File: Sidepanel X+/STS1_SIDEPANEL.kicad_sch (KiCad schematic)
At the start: 3 parts, among them J1 Conn_02x04_Odd_Even, J2 Conn_02x02_Odd_Even

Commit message: Review Ready for V2.0
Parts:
- J1: value Conn_02x04_Odd_Even -> (none); footprint SamacSys:M808280842 -> (none)
- J2: value Conn_02x02_Odd_Even -> (none); footprint USER_Passiv:M80-8280442 -> (none)
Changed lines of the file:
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@@
     (in_bom yes) (on_board yes) (fields_autoplaced)
     (property "Reference" "J1" (id 0) (at 40.64 60.96 0))
-    (property "Value" "Conn_02x04_Odd_Even" (id 1) (at 40.64 63.5 0))
-    (property "Footprint" "SamacSys:M808280842" (id 2) (at 39.37 69.85 0)
+    (property "Value" "" (id 1) (at 40.64 63.5 0))
+    (property "Footprint" "" (id 2) (at 39.37 69.85 0)
       (effects (font (size 1.27 1.27)) hide)
     )
@@
     (in_bom yes) (on_board yes) (fields_autoplaced)
     (property "Reference" "J2" (id 0) (at 86.36 66.04 0))
-    (property "Value" "Conn_02x02_Odd_Even" (id 1) (at 86.36 68.58 0))
-    (property "Footprint" "USER_Passiv:M80-8280442" (id 2) (at 85.09 72.39 0)
+    (property "Value" "" (id 1) (at 86.36 68.58 0))
+    (property "Footprint" "" (id 2) (at 85.09 72.39 0)
       (effects (font (size 1.27 1.27)) hide)
     )
@@
     )
     (path "/4f87559b-6bba-4ff6-97a7-dad9a308db2d/934b6342-5d8d-49da-bf4f-f7fa77f16f34"
-      (reference "CUR1") (unit 1) (value "TMCS1101A3BQDT") (footprint "SOIC127P600X175-8N")
+      (reference "CUR1") (unit 1) (value "TMCS1101A3BQDT") (footprint "Package_SO:SOIC-8_3.9x4.9mm_P1.27mm")
     )
     (path "/4f87559b-6bba-4ff6-97a7-dad9a308db2d/a554cf31-0806-4740-ba0b-f0d59599f4ca"
@@
     )
     (path "/4f87559b-6bba-4ff6-97a7-dad9a308db2d/c6a198d2-e0e4-4d6d-8a2a-bdeb249501be"
-      (reference "DOUT1") (unit 1) (value "SMM4F5.0") (footprint "SamacSys:STMITE")
+      (reference "DOUT1") (unit 1) (value "SMM4F5.0") (footprint "Diode_SMD:D_0603_1608Metric")
     )
     (path "/9d03bb93-a9aa-424f-bd25-022f173efd1d/d9839939-8918-48f3-b4b2-d753b1d9a645"
-      (reference "IC1") (unit 1) (value "TMP112AQDRLRQ1") (footprint "SamacSys:SOTFL50P160X60-6N")
+      (reference "IC1") (unit 1) (value "TMP112AQDRLRQ1") (footprint "Package_TO_SOT_SMD:SOT-563")
     )
     (path "/7d4ab197-adca-450c-9fc5-7a95ff72b885"
-      (reference "J1") (unit 1) (value "Conn_02x04_Odd_Even") (footprint "SamacSys:M808280842")
+      (reference "J1") (unit 1) (value "Conn_02x04_Odd_Even") (footprint "STS_Connector:M808280842")
     )
     (path "/9272ccd5-e950-4f99-baec-47da7f19129b"
-      (reference "J2") (unit 1) (value "Conn_02x02_Odd_Even") (footprint "USER_Passiv:M80-8280442")
+      (reference "J2") (unit 1) (value "Conn_02x02_Odd_Even") (footprint "STS_Connector:M808280442")
     )
     (path "/4f87559b-6bba-4ff6-97a7-dad9a308db2d/bfe4e68f-4cef-4b31-adff-8df094bc3870"
-      (reference "L_IN1") (unit 1) (value "10u") (footprint "SamacSys:INDPM5650X530N")
+      (reference "L_IN1") (unit 1) (value "10u") (footprint "Inductor_SMD:L_0805_2012Metric")
     )
     (path "/4f87559b-6bba-4ff6-97a7-dad9a308db2d/679b2e27-da22-4f13-a86e-25be83598a10"
-      (reference "MPPT1") (unit 1) (value "SPV1040TTR") (footprint "SamacSys:SOP65P640X120-8N")
+      (reference "MPPT1") (unit 1) (value "SPV1040TTR") (footprint "Package_SO:TSSOP-8_4.4x3mm_P0.65mm")
     )
     (path "/6503b427-07c6-4391-8fa6-4757fb4daa6c"
@@
     )
     (path "/4f87559b-6bba-4ff6-97a7-dad9a308db2d/e7b54c2f-482e-4a97-841f-62a80e0193a8"
-      (reference "SC1") (unit 1) (value "Solar_Cell") (footprint "USER_Activ:3G30A_40x80")
+      (reference "SC1") (unit 1) (value "Solar_Cell") (footprint "STS_Connector:3G30A_40x80")
     )
     (path "/9d03bb93-a9aa-424f-bd25-022f173efd1d/a83d6342-0e16-4131-8bb9-e65e4d72dab0"
-      (reference "U1") (unit 1) (value "GUVA-C32SM") (footprint "USER_Optic:OLGA 2mm x 2,3mm")
-    )
-  )
+      (reference "U1") (unit 1) (value "GUVA-C32SM") (footprint "Package_SO:SO-4_4.4x3.6mm_P2.54mm")
+    )
+  )

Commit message: Further fixes, still some open
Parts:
- J1: value (none) -> Conn_02x04_Odd_Even; footprint (none) -> STS_Connector:M808280842
- J2: value (none) -> Conn_02x02_Odd_Even; footprint (none) -> STS_Connector:M808280442
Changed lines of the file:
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@@
     (in_bom yes) (on_board yes) (fields_autoplaced)
     (property "Reference" "J1" (id 0) (at 40.64 60.96 0))
-    (property "Value" "" (id 1) (at 40.64 63.5 0))
-    (property "Footprint" "" (id 2) (at 39.37 69.85 0)
+    (property "Value" "Conn_02x04_Odd_Even" (id 1) (at 40.64 63.5 0))
+    (property "Footprint" "STS_Connector:M808280842" (id 2) (at 39.37 69.85 0)
       (effects (font (size 1.27 1.27)) hide)
     )
@@
     (in_bom yes) (on_board yes) (fields_autoplaced)
     (property "Reference" "J2" (id 0) (at 86.36 66.04 0))
-    (property "Value" "" (id 1) (at 86.36 68.58 0))
-    (property "Footprint" "" (id 2) (at 85.09 72.39 0)
+    (property "Value" "Conn_02x02_Odd_Even" (id 1) (at 86.36 68.58 0))
+    (property "Footprint" "STS_Connector:M808280442" (id 2) (at 85.09 72.39 0)
       (effects (font (size 1.27 1.27)) hide)
     )

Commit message: Next fix
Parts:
- added TH1: Thermistor_NTC, Resistor_SMD:R_0805_2012Metric_Pad1.20x1.40mm_HandSolder, symbol Device:Thermistor_NTC
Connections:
- net GND: now also TH1.2
- net TEMP+: now also TH1.1
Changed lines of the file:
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@@
 (kicad_sch (version 20211123) (generator eeschema)
   (paper "A4")
+  (wire (pts (xy 31.75 88.9) (xy 31.75 92.71))
+    (stroke (width 0) (type default) (color 0 0 0 0))
+  )
+  (wire (pts (xy 31.75 100.33) (xy 31.75 103.505))
+    (stroke (width 0) (type default) (color 0 0 0 0))
+  )
   (wire (pts (xy 26.67 67.31) (xy 34.29 67.31))
     (stroke (width 0) (type default) (color 0 0 0 0))
@@
     (stroke (width 0) (type default) (color 0 0 0 0))
   )
+  (wire (pts (xy 31.75 88.9) (xy 38.735 88.9))
+    (stroke (width 0) (type default) (color 0 0 0 0))
+  )
   (wire (pts (xy 96.52 36.83) (xy 104.14 36.83))
     (stroke (width 0) (type default) (color 0 0 0 0))
@@
     (stroke (width 0) (type default) (color 0 0 0 0))
   )
+  (label "TEMP+" (at 38.735 88.9 180)
+    (effects (font (size 1.27 1.27)) (justify right bottom))
+  )
   (label "SC1_I+" (at 54.61 67.31 180)
     (effects (font (size 1.27 1.27)) (justify right bottom))
@@
   (label "SC2_I+" (at 82.55 41.91 180)
     (effects (font (size 1.27 1.27)) (justify right bottom))
+  )
+  (symbol (lib_id "power:GND") (at 31.75 103.505 0) (unit 1)
+    (in_bom yes) (on_board yes) (fields_autoplaced)
+    (property "Reference" "#PWR0107" (id 0) (at 31.75 109.855 0)
+      (effects (font (size 1.27 1.27)) hide)
+    )
+    (property "Value" "GND" (id 1) (at 31.75 108.585 0))
+    (property "Footprint" "" (id 2) (at 31.75 103.505 0)
+      (effects (font (size 1.27 1.27)) hide)
+    )
+    (property "Datasheet" "" (id 3) (at 31.75 103.505 0)
+      (effects (font (size 1.27 1.27)) hide)
+    )
+    (pin "1")
   )
   (symbol (lib_id "power:GND") (at 58.42 76.2 0) (unit 1)
@@
       (effects (font (size 1.27 1.27)) hide)
     )
+  )
+  (symbol (lib_id "Device:Thermistor_NTC") (at 31.75 96.52 0) (unit 1)
+    (in_bom yes) (on_board yes) (fields_autoplaced)
+    (property "Reference" "TH1" (id 0) (at 34.29 95.5674 0)
+      (effects (font (size 1.27 1.27)) (justify left))
+    )
+    (property "Value" "Thermistor_NTC" (id 1) (at 34.29 98.1074 0)
+      (effects (font (size 1.27 1.27)) (justify left))
+    )
+    (property "Footprint" "Resistor_SMD:R_0805_2012Metric_Pad1.20x1.40mm_HandSolder" (id 2) (at 31.75 95.25 0)
+      (effects (font (size 1.27 1.27)) hide)
+    )
+    (property "Datasheet" "~" (id 3) (at 31.75 95.25 0)
+      (effects (font (size 1.27 1.27)) hide)
+    )
+    (pin "1")
+    (pin "2")
   )
   (symbol (lib_id "Connector_Generic:Conn_02x04_Odd_Even") (at 39.37 69.85 0) (unit 1)
@@
       (reference "#PWR0106") (unit 1) (value "GND") (footprint "")
     )
+    (path "/10dfac46-9067-4751-a078-8b3b3c2c59bd"
+      (reference "#PWR0107") (unit 1) (value "GND") (footprint "")
+    )
     (path "/4f87559b-6bba-4ff6-97a7-dad9a308db2d/5bbe5da1-3bad-4b6d-b046-d5fbf4c349d2"
       (reference "#PWR0108") (unit 1) (value "GND") (footprint "")
@@
     )
     (path "/4f87559b-6bba-4ff6-97a7-dad9a308db2d/e7b54c2f-482e-4a97-841f-62a80e0193a8"
-      (reference "SC1") (unit 1) (value "Solar_Cell") (footprint "STS_Connector:3G30A_40x80")
+      (reference "SC1") (unit 1) (value "Solar_Cell") (footprint "STS_Solarcells:3G30A_40x80")
+    )
+    (path "/750cb84e-d795-4364-9358-ec0975478b7f"
+      (reference "TH1") (unit 1) (value "Thermistor_NTC") (footprint "Resistor_SMD:R_0805_2012Metric_Pad1.20x1.40mm_HandSolder")
     )
     (path "/9d03bb93-a9aa-424f-bd25-022f173efd1d/a83d6342-0e16-4131-8bb9-e65e4d72dab0"

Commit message: release_2.0, Ordered PCBs
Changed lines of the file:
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@@
     )
     (path "/4f87559b-6bba-4ff6-97a7-dad9a308db2d/c6a198d2-e0e4-4d6d-8a2a-bdeb249501be"
-      (reference "DOUT1") (unit 1) (value "SMM4F5.0") (footprint "Diode_SMD:D_0603_1608Metric")
+      (reference "DOUT1") (unit 1) (value "SMM4F5.0") (footprint "SamacSys:STMITE")
     )
     (path "/9d03bb93-a9aa-424f-bd25-022f173efd1d/d9839939-8918-48f3-b4b2-d753b1d9a645"
@@
     )
     (path "/4f87559b-6bba-4ff6-97a7-dad9a308db2d/bfe4e68f-4cef-4b31-adff-8df094bc3870"
-      (reference "L_IN1") (unit 1) (value "10u") (footprint "Inductor_SMD:L_0805_2012Metric")
+      (reference "L_IN1") (unit 1) (value "10u") (footprint "STS_Inductor_SMD:XAL6060103MEC")
     )
     (path "/4f87559b-6bba-4ff6-97a7-dad9a308db2d/679b2e27-da22-4f13-a86e-25be83598a10"

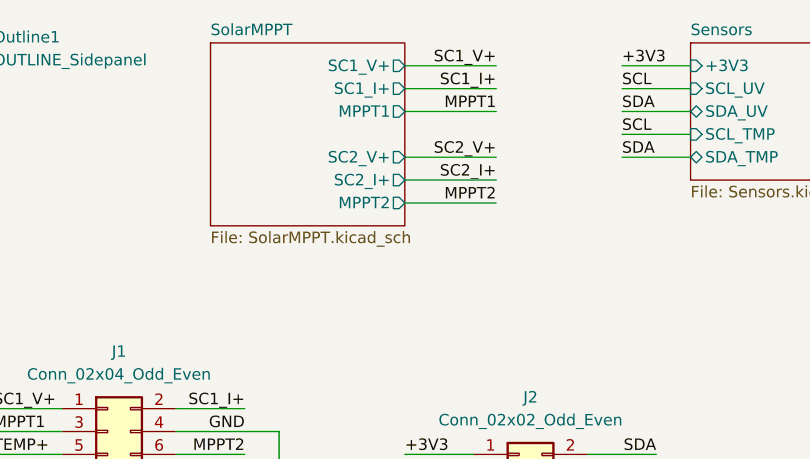
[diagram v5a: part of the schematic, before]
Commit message: Fixed some DRC errors.
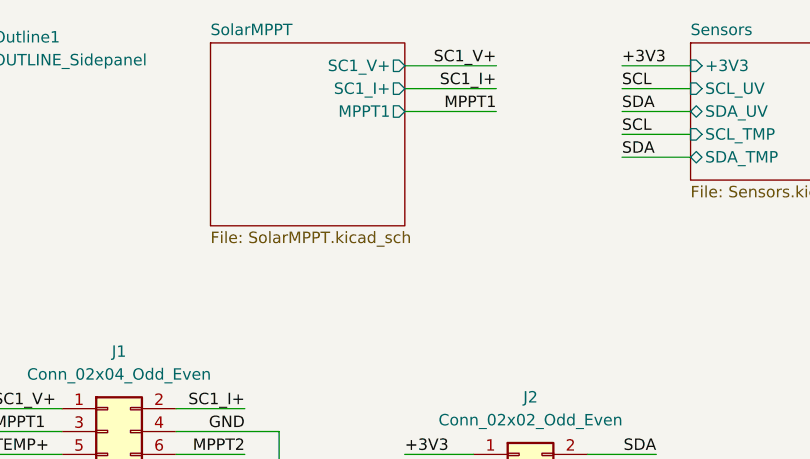
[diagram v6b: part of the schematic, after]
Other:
- sheet SolarMPPT ports: added none; removed MPPT2, SC2_I+, SC2_V+
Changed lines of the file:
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@@
-    (stroke (width 0) (type default) (color 0 0 0 0))
-  )
-  (wire (pts (xy 72.39 39.37) (xy 82.55 39.37))
     (stroke (width 0) (type default) (color 0 0 0 0))
   )
@@
     (stroke (width 0) (type default) (color 0 0 0 0))
   )
-  (wire (pts (xy 72.39 44.45) (xy 82.55 44.45))
-    (stroke (width 0) (type default) (color 0 0 0 0))
-  )
   (wire (pts (xy 96.52 34.29) (xy 104.14 34.29))
     (stroke (width 0) (type default) (color 0 0 0 0))
@@
     (stroke (width 0) (type default) (color 0 0 0 0))
   )
-  (wire (pts (xy 72.39 41.91) (xy 82.55 41.91))
-    (stroke (width 0) (type default) (color 0 0 0 0))
-  )
   (wire (pts (xy 46.99 69.85) (xy 58.42 69.85))
     (stroke (width 0) (type default) (color 0 0 0 0))
@@
     (effects (font (size 1.27 1.27)) (justify right bottom))
   )
-  (label "MPPT2" (at 82.55 44.45 180)
-    (effects (font (size 1.27 1.27)) (justify right bottom))
-  )
   (label "MPPT1" (at 26.67 69.85 0)
     (effects (font (size 1.27 1.27)) (justify left bottom))
@@
     (effects (font (size 1.27 1.27)) (justify right bottom))
   )
-  (label "SC2_V+" (at 82.55 39.37 180)
-    (effects (font (size 1.27 1.27)) (justify right bottom))
-  )
   (label "SC2_V+" (at 54.61 74.93 180)
     (effects (font (size 1.27 1.27)) (justify right bottom))
@@
   )
   (label "SDA" (at 100.33 72.39 180)
-    (effects (font (size 1.27 1.27)) (justify right bottom))
-  )
-  (label "SC2_I+" (at 82.55 41.91 180)
     (effects (font (size 1.27 1.27)) (justify right bottom))
   )
@@
       (effects (font (size 1.27 1.27)) (justify left top))
     )
-    (pin "SC2_I+" output (at 72.39 41.91 0)
-      (effects (font (size 1.27 1.27)) (justify right))
-    )
-    (pin "MPPT2" output (at 72.39 44.45 0)
-      (effects (font (size 1.27 1.27)) (justify right))
-    )
     (pin "SC1_V+" output (at 72.39 29.21 0)
       (effects (font (size 1.27 1.27)) (justify right))
@@
       (effects (font (size 1.27 1.27)) (justify right))
     )
-    (pin "SC2_V+" output (at 72.39 39.37 0)
-      (effects (font (size 1.27 1.27)) (justify right))
-    )

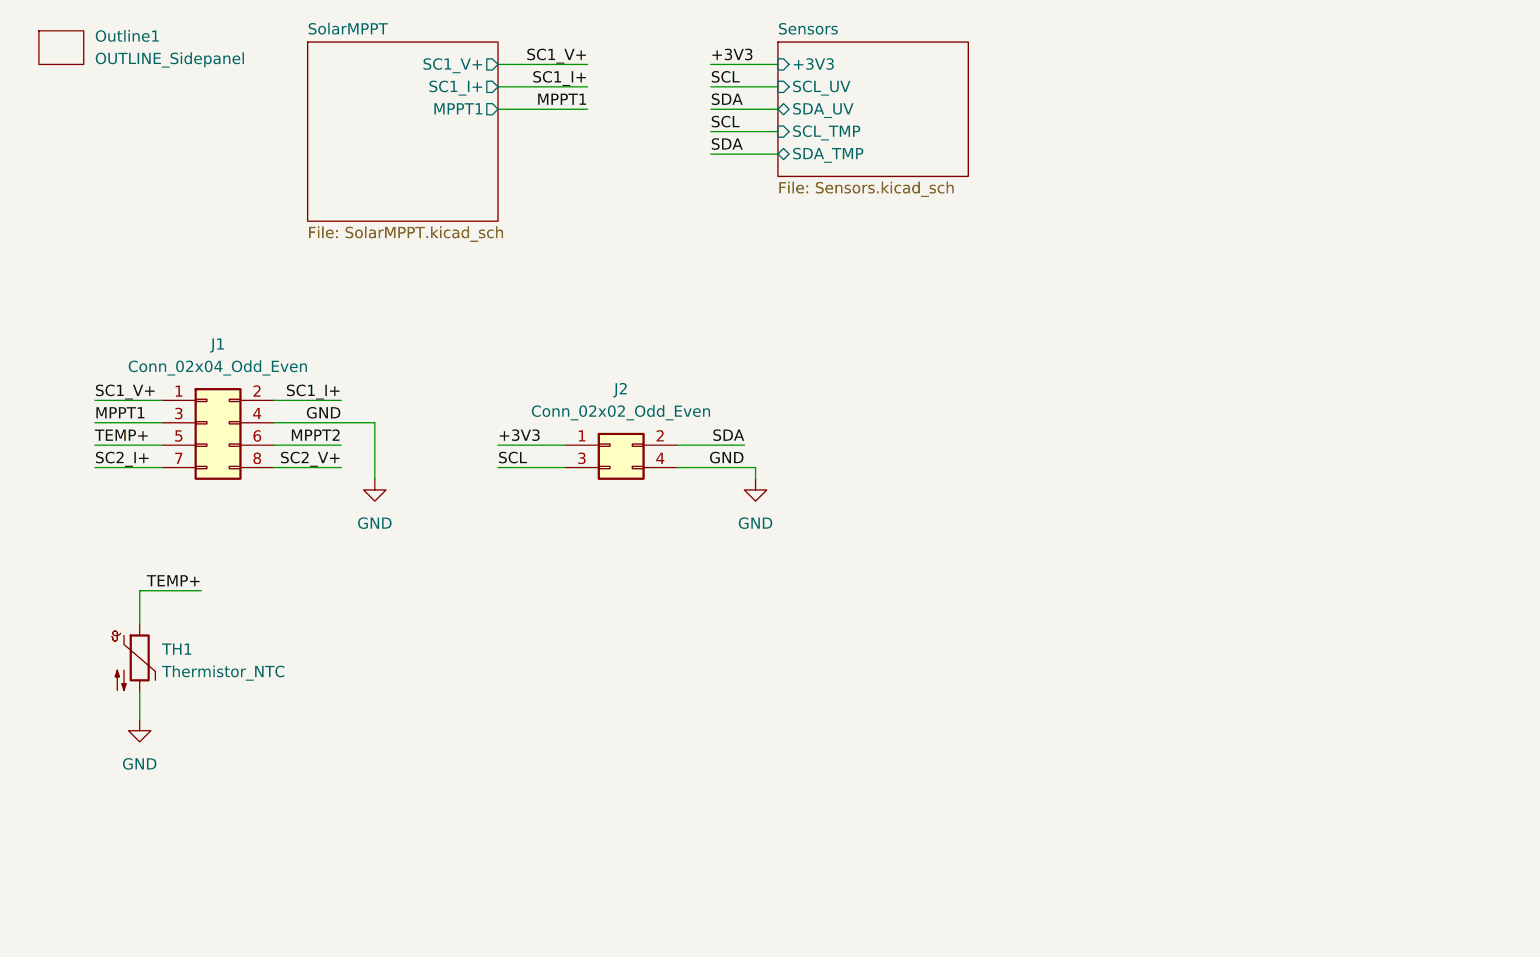
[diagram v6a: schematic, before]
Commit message: changes to the solar cells footprint, added camera mounts
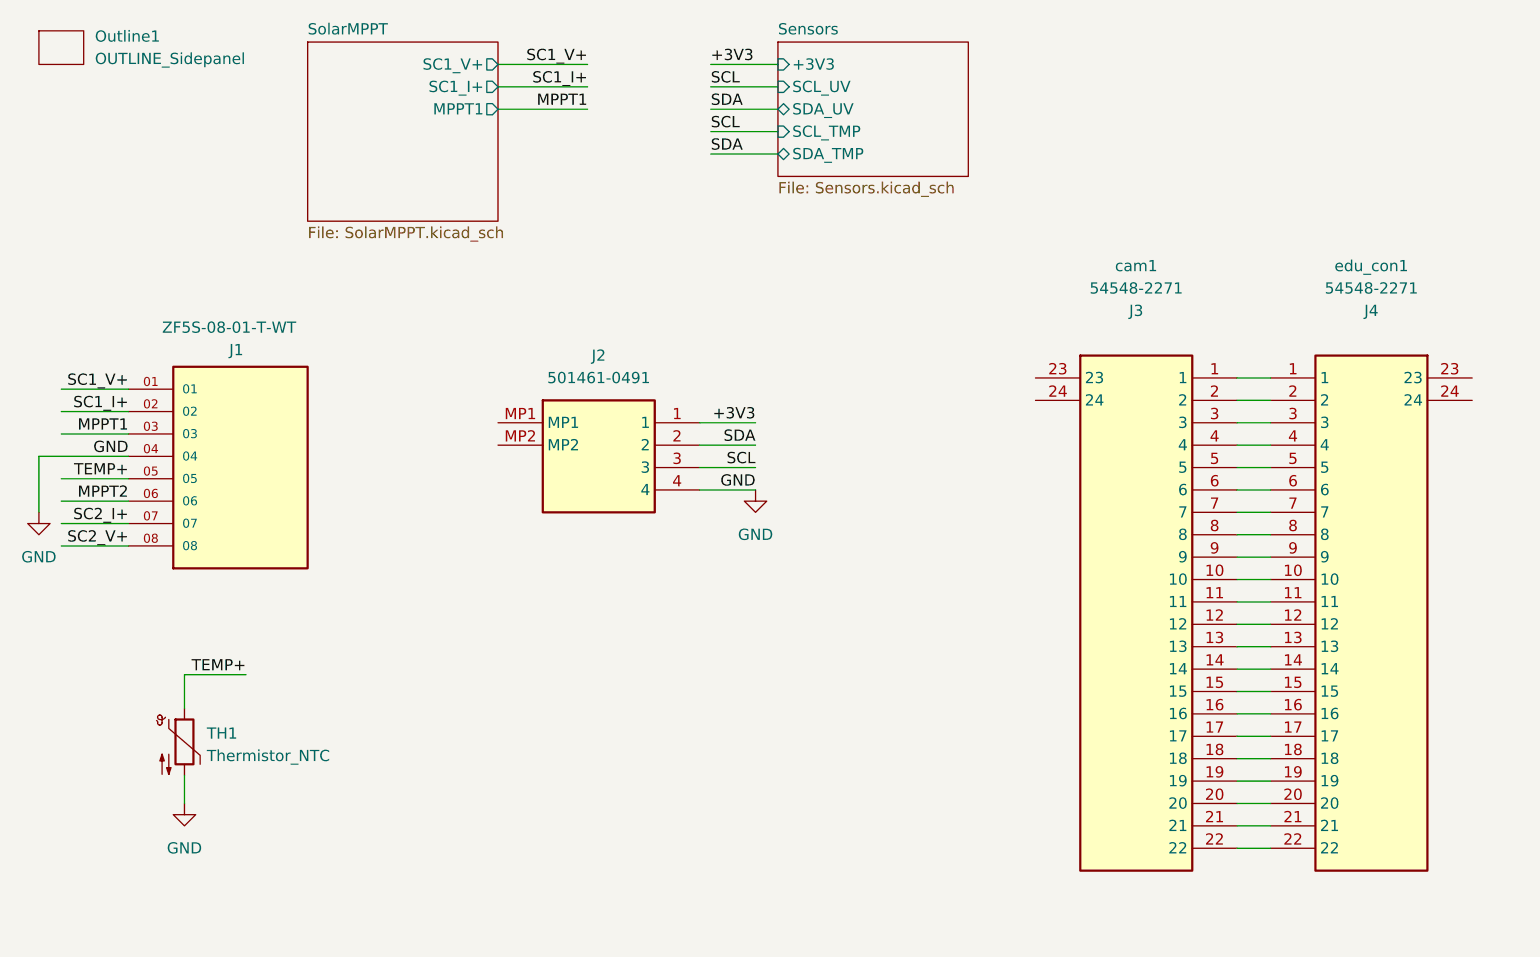
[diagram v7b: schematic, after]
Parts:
- removed J1: Conn_02x04_Odd_Even, STS_Connector:M808280842, symbol Connector_Generic:Conn_02x04_Odd_Even
- removed J2: Conn_02x02_Odd_Even, STS_Connector:M808280442, symbol Connector_Generic:Conn_02x02_Odd_Even
- added J1: ZF5S-08-01-T-WT, Sts:SAMTEC_ZF5S-08-01-T-WT, symbol EPS connector:ZF5S-08-01-T-WT
- added UV1: 501461-0491, Sts:5014610491, symbol Connector:501461-0491
- added cam1, edu_con1: 54548-2271, Sts:545482271, symbol Cam:54548-2271
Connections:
- net +3V3: now also UV1.1
- net GND: now also J1.04, UV1.4
- net MPPT1: now also J1.03
- net MPPT2: now also J1.06
- net SC1_I+: now also J1.02
- net SC1_V+: now also J1.01
- net SC2_I+: now also J1.07
- net SC2_V+: now also J1.08
- net SCL: now also UV1.3
- net SDA: now also UV1.2
- net TEMP+: now also J1.05
- new net: cam1.1, edu_con1.1
- new net: cam1.10, edu_con1.10
- new net: cam1.11, edu_con1.11
- new net: cam1.12, edu_con1.12
- new net: cam1.13, edu_con1.13
- new net: cam1.14, edu_con1.14
- new net: cam1.15, edu_con1.15
- new net: cam1.16, edu_con1.16
- new net: cam1.17, edu_con1.17
- new net: cam1.18, edu_con1.18
- new net: cam1.19, edu_con1.19
- new net: cam1.2, edu_con1.2
- new net: cam1.20, edu_con1.20
- new net: cam1.21, edu_con1.21
- new net: cam1.22, edu_con1.22
- new net: cam1.3, edu_con1.3
- new net: cam1.4, edu_con1.4
- new net: cam1.5, edu_con1.5
- new net: cam1.6, edu_con1.6
- new net: cam1.7, edu_con1.7
- new net: cam1.8, edu_con1.8
- new net: cam1.9, edu_con1.9
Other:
- moved on the sheet: TH1

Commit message: small adjustments
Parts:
- removed J1: ZF5S-08-01-T-WT, Sts:SAMTEC_ZF5S-08-01-T-WT, symbol EPS connector:ZF5S-08-01-T-WT
- removed cam1, edu_con1: 54548-2271, Sts:545482271, symbol Cam:54548-2271
- added J1: Conn_01x08, STS_connector:SAMTEC_ZF5S-08-01-T-WT, symbol Connector_Generic:Conn_01x08
- added cam2, edu_con2: 54548-2271, STS_connector:545482271, symbol Cam:54548-2271
- Outline1: footprint USER_OUTLINE:OUTLINE_SidepanelX+ -> USER_OUTLINE:OUTLINE_SidepanelX-
- UV1: footprint Sts:5014610491 -> STS_connector:5014610491
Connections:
- net GND: now also J1.04 (Pin_4)
- net MPPT1: now also J1.03 (Pin_3)
- net MPPT2: now also J1.06 (Pin_6)
- net SC1_I+: now also J1.02 (Pin_2)
- net SC1_V+: now also J1.01 (Pin_1)
- net SC2_I+: now also J1.07 (Pin_7)
- net SC2_V+: now also J1.08 (Pin_8)
- net TEMP+: now also J1.05 (Pin_5)
- new net: cam2.1, edu_con2.1
- new net: cam2.10, edu_con2.10
- new net: cam2.11, edu_con2.11
- new net: cam2.12, edu_con2.12
- new net: cam2.13, edu_con2.13
- new net: cam2.14, edu_con2.14
- new net: cam2.15, edu_con2.15
- new net: cam2.16, edu_con2.16
- new net: cam2.17, edu_con2.17
- new net: cam2.18, edu_con2.18
- new net: cam2.19, edu_con2.19
- new net: cam2.2, edu_con2.2
- new net: cam2.20, edu_con2.20
- new net: cam2.21, edu_con2.21
- new net: cam2.22, edu_con2.22
- new net: cam2.3, edu_con2.3
- new net: cam2.4, edu_con2.4
- new net: cam2.5, edu_con2.5
- new net: cam2.6, edu_con2.6
- new net: cam2.7, edu_con2.7
- new net: cam2.8, edu_con2.8
- new net: cam2.9, edu_con2.9
- no-connect marks 0 -> 6
